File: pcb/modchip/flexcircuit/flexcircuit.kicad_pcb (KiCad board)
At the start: 2 copper layers, 46.2 x 16.6 mm, 7 parts, among them J2 Conn_01x05_Pin, U1 M2003FC1AE, U2 CK3866SL

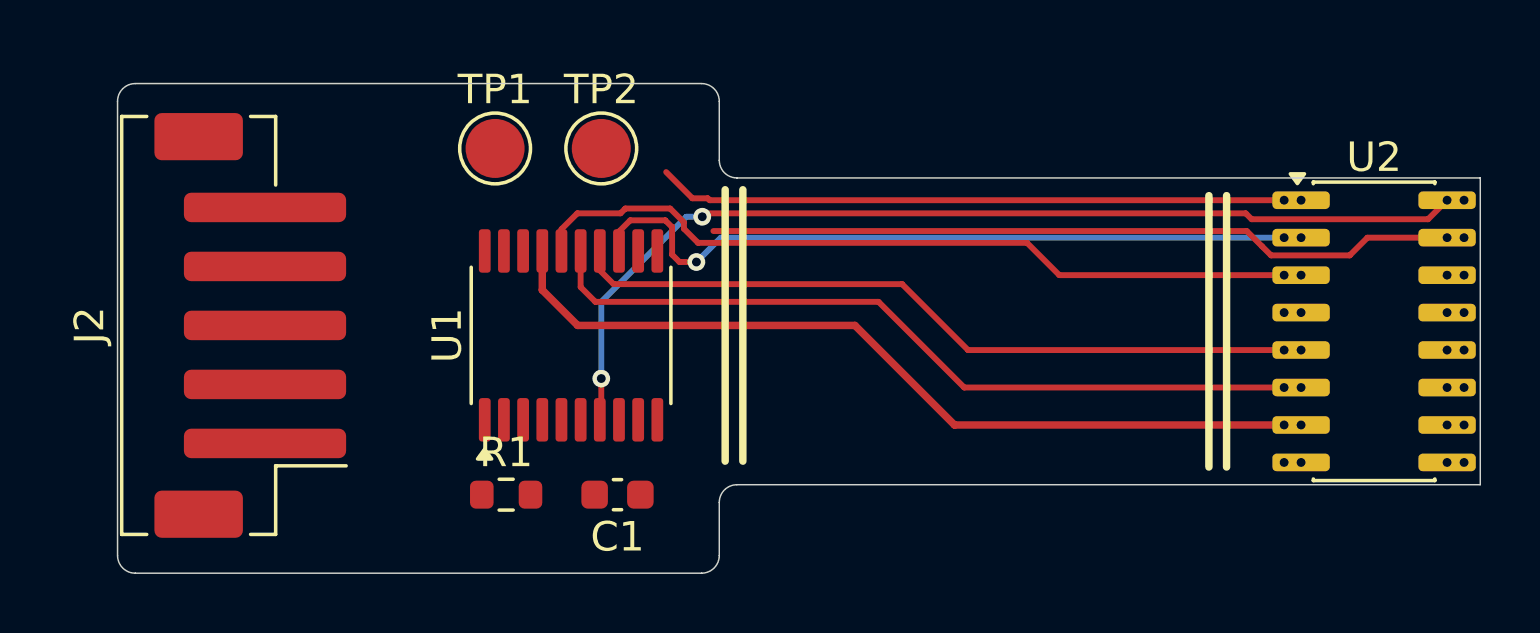
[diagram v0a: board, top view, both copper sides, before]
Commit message: flex circuit as ordered
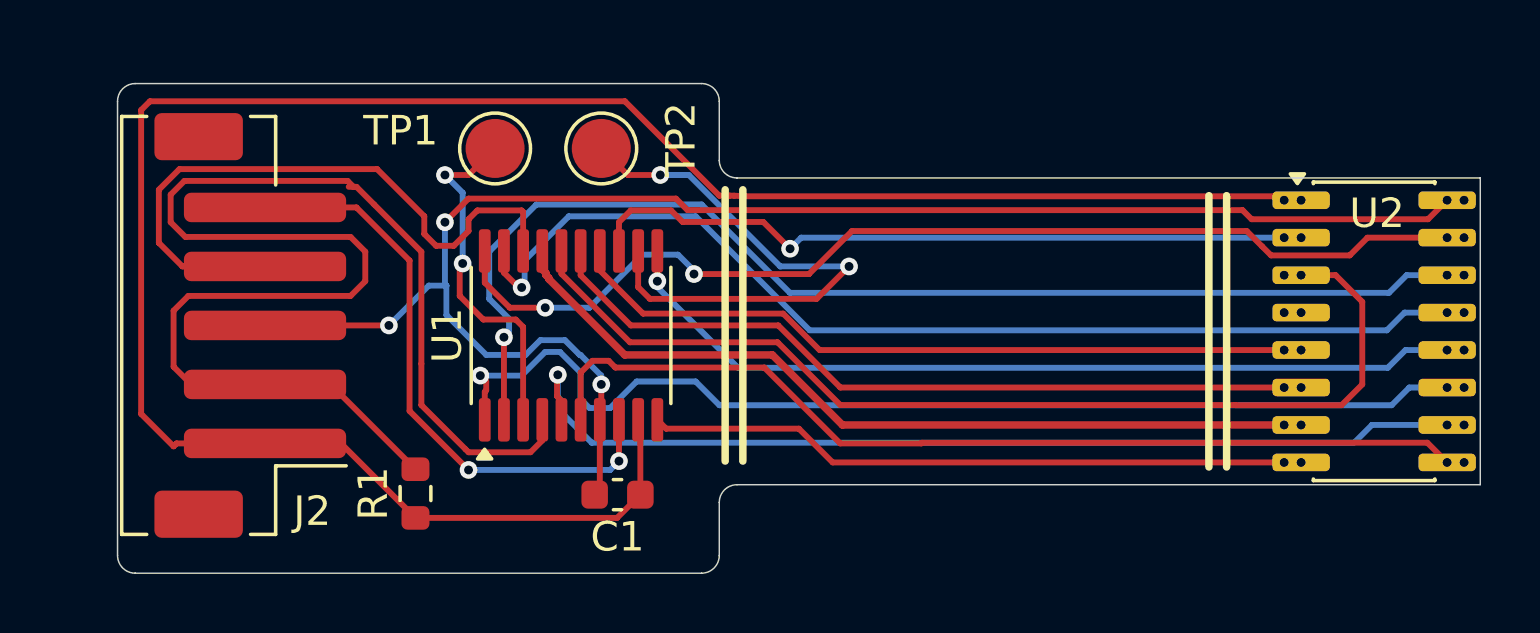
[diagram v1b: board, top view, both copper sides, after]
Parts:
- moved R1 3.08 mm to (106.7, 99.5), turned to 90 degrees
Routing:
- net +5V: track 21.9 -> 72.5 mm
- net /RESET: track 0.00 -> 48.1 mm
- net /I_SENS: track 0.00 -> 40.7 mm, vias 0 -> 1
- net /TACH: track 0.00 -> 37.0 mm, vias 0 -> 1
- net /CT: track 0.00 -> 36.2 mm, vias 0 -> 1
- net /HALL_C: track 0.00 -> 33.7 mm, vias 0 -> 1
- net /HALL_B: track 0.00 -> 32.6 mm
- net /DIR: track 0.00 -> 29.4 mm, vias 0 -> 1
- net /HALL_A: track 0.00 -> 22.4 mm
- net /SWCLK: track 0.00 -> 21.9 mm
- net GND: track 34.3 -> 55.4 mm, vias 2 -> 3
- net /SWDIO: track 0.00 -> 20.2 mm, vias 0 -> 2
- net /PB14: track 0.00 -> 19.1 mm, vias 0 -> 2
- net /PB3: track 0.00 -> 12.3 mm, vias 0 -> 2
- net /PWM: track 25.5 -> 36.4 mm, vias 0 -> 2
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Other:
- board text added: "stiffener"
